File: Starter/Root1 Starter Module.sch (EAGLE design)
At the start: 2 parts

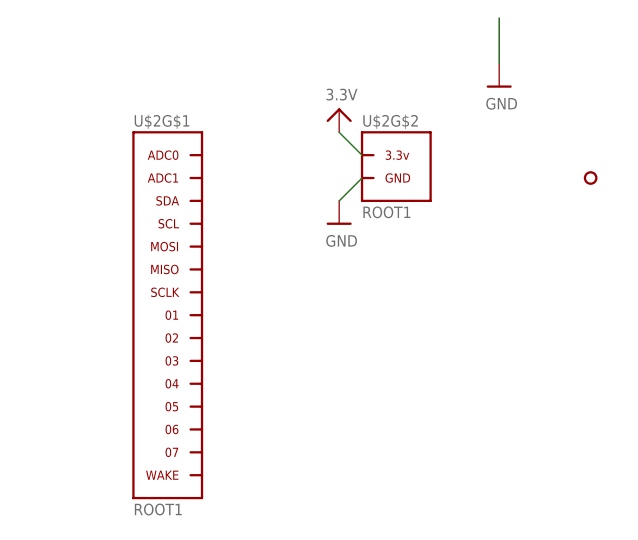
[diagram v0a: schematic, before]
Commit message: Root1 Starter Module:  - Updated connectors  - Dual sided  - Dual #2 screw holes
Signed-off-by: Cruz Monrreal II <Cruz.Monrreal@gmail.com>
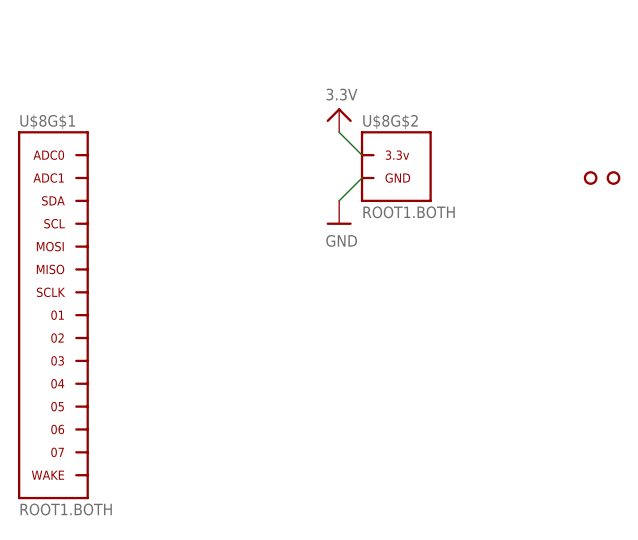
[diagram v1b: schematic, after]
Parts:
- removed U$2: ROOT1, thinkmaketest:ROOT1
- added U$3: HOLE.2MM, .screw_holes:HOLE.2MM
- added U$8: ROOT1.BOTH, thinkmaketest:ROOT1.BOTH
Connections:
- net 3.3V: now also U$8G$2.3.3V; no longer U$2G$2.3.3V
- net GND: now also U$8G$2.GND; no longer U$2G$2.GND
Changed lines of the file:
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@@
 <grid distance="0.1" unitdist="inch" unit="inch" style="lines" multiple="1" display="no" altdistance="0.01" altunitdist="inch" altunit="inch"/>
 <layers>
-<layer number="1" name="Top" color="4" fill="1" visible="yes" active="no"/>
-<layer number="16" name="Bottom" color="1" fill="1" visible="yes" active="no"/>
-<layer number="17" name="Pads" color="2" fill="1" visible="yes" active="no"/>
-<layer number="18" name="Vias" color="2" fill="1" visible="yes" active="no"/>
-<layer number="19" name="Unrouted" color="6" fill="1" visible="yes" active="no"/>
-<layer number="20" name="Dimension" color="15" fill="1" visible="yes" active="no"/>
-<layer number="21" name="tPlace" color="7" fill="1" visible="yes" active="no"/>
-<layer number="22" name="bPlace" color="7" fill="1" visible="yes" active="no"/>
-<layer number="23" name="tOrigins" color="15" fill="1" visible="yes" active="no"/>
-<layer number="24" name="bOrigins" color="15" fill="1" visible="yes" active="no"/>
-<layer number="25" name="tNames" color="7" fill="1" visible="yes" active="no"/>
-<layer number="26" name="bNames" color="7" fill="1" visible="yes" active="no"/>
-<layer number="27" name="tValues" color="7" fill="1" visible="yes" active="no"/>
-<layer number="28" name="bValues" color="7" fill="1" visible="yes" active="no"/>
+<layer number="1" name="Top" color="4" fill="1" visible="no" active="no"/>
+<layer number="16" name="Bottom" color="1" fill="1" visible="no" active="no"/>
+<layer number="17" name="Pads" color="2" fill="1" visible="no" active="no"/>
+<layer number="18" name="Vias" color="2" fill="1" visible="no" active="no"/>
+<layer number="19" name="Unrouted" color="6" fill="1" visible="no" active="no"/>
+<layer number="20" name="Dimension" color="15" fill="1" visible="no" active="no"/>
+<layer number="21" name="tPlace" color="7" fill="1" visible="no" active="no"/>
+<layer number="22" name="bPlace" color="7" fill="1" visible="no" active="no"/>
+<layer number="23" name="tOrigins" color="15" fill="1" visible="no" active="no"/>
+<layer number="24" name="bOrigins" color="15" fill="1" visible="no" active="no"/>
+<layer number="25" name="tNames" color="7" fill="1" visible="no" active="no"/>
+<layer number="26" name="bNames" color="7" fill="1" visible="no" active="no"/>
+<layer number="27" name="tValues" color="7" fill="1" visible="no" active="no"/>
+<layer number="28" name="bValues" color="7" fill="1" visible="no" active="no"/>
 <layer number="29" name="tStop" color="7" fill="3" visible="no" active="no"/>
 <layer number="30" name="bStop" color="7" fill="6" visible="no" active="no"/>
@@
 <layer number="35" name="tGlue" color="7" fill="4" visible="no" active="no"/>
 <layer number="36" name="bGlue" color="7" fill="5" visible="no" active="no"/>
-<layer number="37" name="tTest" color="7" fill="1" visible="yes" active="no"/>
-<layer number="38" name="bTest" color="7" fill="1" visible="yes" active="no"/>
+<layer number="37" name="tTest" color="7" fill="1" visible="no" active="no"/>
+<layer number="38" name="bTest" color="7" fill="1" visible="no" active="no"/>
 <layer number="39" name="tKeepout" color="4" fill="11" visible="no" active="no"/>
 <layer number="40" name="bKeepout" color="1" fill="11" visible="no" active="no"/>
@@
 <layer number="44" name="Drills" color="7" fill="1" visible="no" active="no"/>
 <layer number="45" name="Holes" color="7" fill="1" visible="no" active="no"/>
-<layer number="46" name="Milling" color="3" fill="1" visible="yes" active="no"/>
-<layer number="47" name="Measures" color="7" fill="1" visible="yes" active="no"/>
-<layer number="48" name="Document" color="7" fill="1" visible="yes" active="no"/>
-<layer number="49" name="Reference" color="7" fill="1" visible="yes" active="no"/>
-<layer number="50" name="dxf" color="7" fill="1" visible="yes" active="no"/>
-<layer number="51" name="tDocu" color="7" fill="1" visible="yes" active="no"/>
-<layer number="52" name="bDocu" color="7" fill="1" visible="yes" active="no"/>
-<layer number="53" name="tGND_GNDA" color="7" fill="9" visible="yes" active="no"/>
-<layer number="54" name="bGND_GNDA" color="1" fill="9" visible="yes" active="no"/>
-<layer number="56" name="wert" color="7" fill="1" visible="yes" active="no"/>
+<layer number="46" name="Milling" color="3" fill="1" visible="no" active="no"/>
+<layer number="47" name="Measures" color="7" fill="1" visible="no" active="no"/>
+<layer number="48" name="Document" color="7" fill="1" visible="no" active="no"/>
+<layer number="49" name="Reference" color="7" fill="1" visible="no" active="no"/>
+<layer number="50" name="dxf" color="7" fill="1" visible="no" active="no"/>
+<layer number="51" name="tDocu" color="7" fill="1" visible="no" active="no"/>
+<layer number="52" name="bDocu" color="7" fill="1" visible="no" active="no"/>
+<layer number="53" name="tGND_GNDA" color="7" fill="9" visible="no" active="no"/>
+<layer number="54" name="bGND_GNDA" color="1" fill="9" visible="no" active="no"/>
+<layer number="56" name="wert" color="7" fill="1" visible="no" active="no"/>
 <layer number="91" name="Nets" color="2" fill="1" visible="yes" active="yes"/>
 <layer number="92" name="Busses" color="1" fill="1" visible="yes" active="yes"/>
@@
 <part name="U$5" library="microbuilder" deviceset="GND" device=""/>
 <part name="U$6" library="microbuilder" deviceset="3.3V" device=""/>
-<part name="U$7" library="microbuilder" deviceset="GND" device=""/>
-<part name="U$2" library="thinkmaketest" deviceset="ROOT1" device=""/>
+<part name="U$3" library=".screw_holes" deviceset="HOLE" device=".2MM"/>
+<part name="U$8" library="thinkmaketest" deviceset="ROOT1" device=".BOTH"/>
 </parts>
 <sheets>
@@
 <instance part="U$5" gate="G$1" x="203.2" y="121.92"/>
 <instance part="U$6" gate="G$1" x="203.2" y="132.08"/>
-<instance part="U$7" gate="G$1" x="220.98" y="137.16"/>
-<instance part="U$2" gate="G$1" x="185.42" y="111.76"/>
-<instance part="U$2" gate="G$2" x="210.82" y="127"/>
+<instance part="U$3" gate="G$1" x="233.68" y="127"/>
+<instance part="U$8" gate="G$1" x="172.72" y="111.76"/>
+<instance part="U$8" gate="G$2" x="210.82" y="127"/>
 </instances>
 <busses>
@@
 <net name="GND" class="0">
 <segment>
-<wire x1="220.98" y1="144.78" x2="220.98" y2="139.7" width="0.1524" layer="91"/>
-<pinref part="U$7" gate="G$1" pin="GND"/>
-</segment>
-<segment>
-<pinref part="U$2" gate="G$2" pin="GND"/>
 <pinref part="U$5" gate="G$1" pin="GND"/>
-<wire x1="205.74" y1="127" x2="203.2" y2="124.46" width="0.1524" layer="91"/>
+<pinref part="U$8" gate="G$2" pin="GND"/>
+<wire x1="203.2" y1="124.46" x2="205.74" y2="127" width="0.1524" layer="91"/>
 </segment>
 </net>
 <net name="3.3V" class="0">
 <segment>
-<pinref part="U$2" gate="G$2" pin="3.3V"/>
+<pinref part="U$8" gate="G$2" pin="3.3V"/>
 <pinref part="U$6" gate="G$1" pin="3.3V"/>
 <wire x1="205.74" y1="129.54" x2="203.2" y2="132.08" width="0.1524" layer="91"/>

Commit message: Updated Starter Module w/ standard location and new connector spacing
Signed-off-by: Cruz Monrreal II <Cruz.Monrreal@gmail.com>
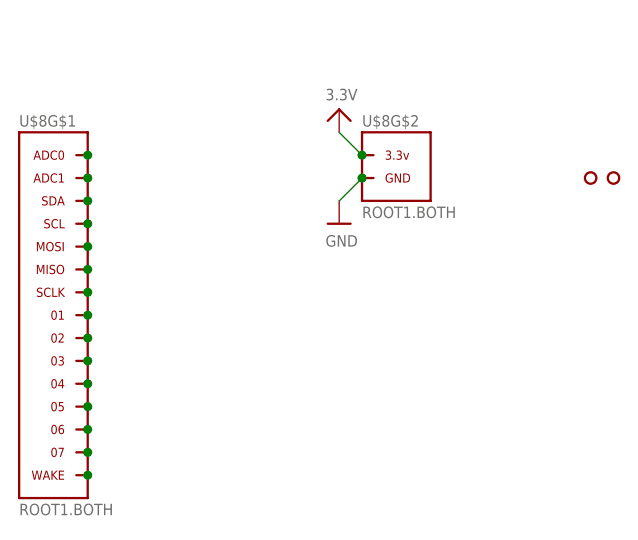
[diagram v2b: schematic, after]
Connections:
- new net N$1: U$8G$1.ADC0
- new net N$10: U$8G$1.03
- new net N$11: U$8G$1.04
- new net N$12: U$8G$1.05
- new net N$13: U$8G$1.06
- new net N$14: U$8G$1.07
- new net N$15: U$8G$1.WAKE
- new net N$2: U$8G$1.ADC1
- new net N$3: U$8G$1.SDA
- new net N$4: U$8G$1.SCL
- new net N$5: U$8G$1.MOSI
- new net N$6: U$8G$1.MISO
- new net N$7: U$8G$1.SCLK
- new net N$8: U$8G$1.01
- new net N$9: U$8G$1.02
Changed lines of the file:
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@@
 <?xml version="1.0" encoding="utf-8"?>
 <!DOCTYPE eagle SYSTEM "eagle.dtd">
-<eagle version="6.2">
+<eagle version="6.1">
 <drawing>
 <settings>
@@
 <pinref part="U$8" gate="G$2" pin="GND"/>
 <wire x1="203.2" y1="124.46" x2="205.74" y2="127" width="0.1524" layer="91"/>
+<junction x="205.74" y="127"/>
 </segment>
 </net>
@@
 <pinref part="U$6" gate="G$1" pin="3.3V"/>
 <wire x1="205.74" y1="129.54" x2="203.2" y2="132.08" width="0.1524" layer="91"/>
-</segment>
-</net>
+<junction x="205.74" y="129.54"/>
+</segment>
+</net>
+<net name="N$1" class="0">
+<segment>
+<pinref part="U$8" gate="G$1" pin="ADC0"/>
+<junction x="175.26" y="129.54"/>
+</segment>
+</net>
+<net name="N$2" class="0">
+<segment>
+<pinref part="U$8" gate="G$1" pin="ADC1"/>
+<junction x="175.26" y="127"/>
+</segment>
+</net>
+<net name="N$3" class="0">
+<segment>
+<pinref part="U$8" gate="G$1" pin="SDA"/>
+<junction x="175.26" y="124.46"/>
+</segment>
+</net>
+<net name="N$4" class="0">
+<segment>
+<pinref part="U$8" gate="G$1" pin="SCL"/>
+<junction x="175.26" y="121.92"/>
+</segment>
+</net>
+<net name="N$5" class="0">
+<segment>
+<pinref part="U$8" gate="G$1" pin="MOSI"/>
+<junction x="175.26" y="119.38"/>
+</segment>
+</net>
+<net name="N$6" class="0">
+<segment>
+<pinref part="U$8" gate="G$1" pin="MISO"/>
+<junction x="175.26" y="116.84"/>
+</segment>
+</net>
+<net name="N$7" class="0">
+<segment>
+<pinref part="U$8" gate="G$1" pin="SCLK"/>
+<junction x="175.26" y="114.3"/>
+</segment>
+</net>
+<net name="N$8" class="0">
+<segment>
+<pinref part="U$8" gate="G$1" pin="01"/>
+<junction x="175.26" y="111.76"/>
+</segment>
+</net>
+<net name="N$9" class="0">
+<segment>
+<pinref part="U$8" gate="G$1" pin="02"/>
+<junction x="175.26" y="109.22"/>
+</segment>
+</net>
+<net name="N$10" class="0">
+<segment>
+<pinref part="U$8" gate="G$1" pin="03"/>
+<junction x="175.26" y="106.68"/>
+</segment>
+</net>
+<net name="N$11" class="0">
+<segment>
+<pinref part="U$8" gate="G$1" pin="04"/>
+<junction x="175.26" y="104.14"/>
+</segment>
+</net>
+<net name="N$12" class="0">
+<segment>
+<pinref part="U$8" gate="G$1" pin="05"/>
+<junction x="175.26" y="101.6"/>
+</segment>
+</net>
+<net name="N$13" class="0">
+<segment>
+<pinref part="U$8" gate="G$1" pin="06"/>
+<junction x="175.26" y="99.06"/>
+</segment>
+</net>
+<net name="N$14" class="0">
+<segment>
+<pinref part="U$8" gate="G$1" pin="07"/>
+<junction x="175.26" y="96.52"/>
+</segment>
+</net>
+<net name="N$15" class="0">
+<segment>
+<pinref part="U$8" gate="G$1" pin="WAKE"/>
+<junction x="175.26" y="93.98"/>
+</segment>
+</net>
